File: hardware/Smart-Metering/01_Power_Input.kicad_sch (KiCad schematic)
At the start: 0 parts

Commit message: Implementa folha de entrada de energia e numera referências por folha
01_Power_Input:
- modo padrão: LINE_A/B/C -> fusível -> diodo S1M em OU para o
  barramento HV, retorno no NEUTRAL via JP101; o instrumento segue
  alimentado com qualquer fase presente;
- modo auxiliar (J101, 100-240 VAC, com varistor): F104/D104/JP102,
  não montados por padrão; para rede 3 fios sem neutro;
- R101 fusível limita inrush, C101 4,7 uF/450 V no barramento;
- PS101 módulo AC/DC isolado 5 V / 2 A (ex.: IRM-10-5) gerando
  VIN_ACDC para a folha 09, referenciado a GND_SYS.

Referências renumeradas por folha para evitar colisões: folha 02 passa
a 2xx (R201 = ligação neutro/GND), folha 03 a 3xx e folha 04 a 4xx
(U401 = ADE9430).

Novos símbolos: D_Rect, CP_Vert, Jumper_2 e ACDC_Module.

Co-Authored-By: Claude Opus 5.5 <noreply@anthropic.com>
Claude-Session: https://claude.ai/code/session_012B8cVkhtjf3eg98UdpNCpf
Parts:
- added C101: 4.7uF 450V, Capacitor_THT:CP_Radial_D8.0mm_P3.50mm, symbol SmartMetering:CP_Vert
- added C102: 22uF, Capacitor_SMD:C_1206_3216Metric, symbol SmartMetering:C_Vert
- added C103: 100nF, Capacitor_SMD:C_0603_1608Metric, symbol SmartMetering:C_Vert
- added D101, D102, D103, D104: S1M, Diode_SMD:D_SMA, symbol SmartMetering:D_Rect
- added F101, F102, F103, F104: T250mA 500VAC, symbol SmartMetering:Fuse
- added J101: AUX L N, TerminalBlock_Phoenix:TerminalBlock_Phoenix_MKDS-1,5-2-5.08_1x02_P5.08mm_Horizontal, symbol SmartMetering:Screw_Terminal_01x02
- added JP101, JP102: LINK, Resistor_THT:R_Axial_DIN0207_L6.3mm_D2.5mm_P7.62mm_Horizontal, symbol SmartMetering:Jumper_2
- added PS101: IRM-10-5, symbol SmartMetering:ACDC_Module
- added R101: 22R 2W, Resistor_THT:R_Axial_DIN0414_L11.9mm_D4.5mm_P15.24mm_Horizontal, symbol SmartMetering:R_Vert
- added RV101: 320VAC 14mm, symbol SmartMetering:Varistor
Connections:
- new net: C101.1 (+), PS101.1 (AC/L), R101.2
- new net: D103.2 (A), F103.2
- new net: D101.1 (K), D102.1 (K), D103.1 (K), D104.1 (K), R101.1
- new net: D102.2 (A), F102.2
- new net: D104.2 (A), F104.2
- new net: D101.2 (A), F101.2
- new net GND_SYS: C102.2, C103.2, PS101.3 (-V)
- new net HV_RTN: C101.2 (-), JP101.2, JP102.2, PS101.2 (AC/N)
- new net LINE_A: F101.1
- new net LINE_B: F102.1
- new net LINE_C: F103.1
- new net L_AUX: F104.1, J101.1, RV101.1
- new net NEUTRAL: JP101.1
- new net N_AUX: J101.2, JP102.1, RV101.2
- new net VIN_ACDC: C102.1, C103.1, PS101.4 (+V)
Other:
- note added: "ENTRADA DE ENERGIA DO INSTRUMENTO Modo padrão (pelas fases medidas): F101-F103 + D101-D103 + JP101 montados; F104/D104/JP102 não montados. O instrumento continua alimentado enquanto houver qualquer fase presente (OU de diodos, retorno no NEUTRO). Barramento HV ≈ 311 VDC com 220 V fase-neutro. Modo auxiliar (J101, 100-240 VAC): F104 + D104 + JP102 montados; F101-F103 e JP101 não montados. Use em r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"
- note added: "PS101: módulo AC/DC isolado (reforçado), 5 V / 2 A, aceita entrada CC 120-370 V. Ele é a barreira de isolação entre a rede e o domínio seguro (GND_SYS). Confirmar isolação e categoria de sobretensão do módulo para CAT III 300 V; a proteção de surto vem dos varistores (folha 02 e RV101) e de R101 (fusível, limita inrush). R101 e C101: limitam a corrente de partida e filtram o ripple do retificador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"
- company: (none) -> Smart-Metering
- title: (none) -> Power Input - AC/DC

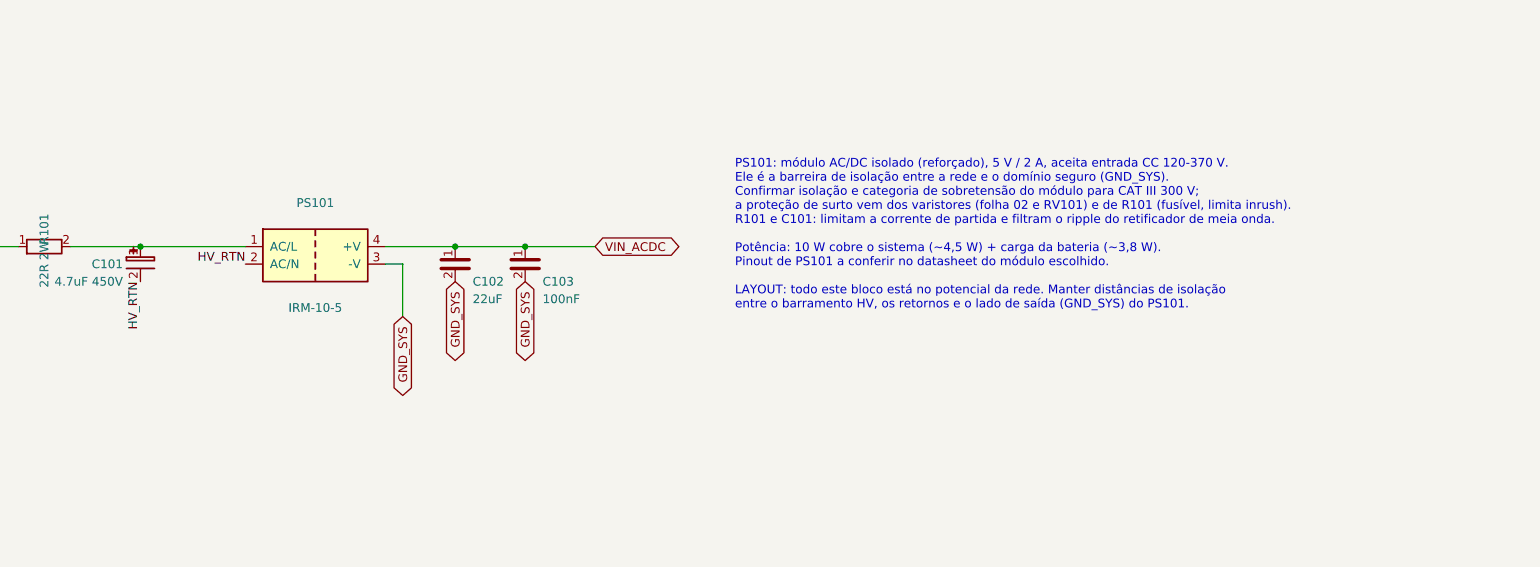
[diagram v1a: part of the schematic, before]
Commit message: Revisão completa do esquemático e correções
Verificação automática sobre o netlist global (215 componentes, 176 nets):
sem pinos soltos, sem nets de alimentação sem fonte, sem saídas em
conflito e isolação íntegra (terras só se encontram nas barreiras
PS101, PS601, U601, U602 e U801).

Correções:
- footprint do ADE9430 inexistente na biblioteca KiCad trocado por
  QFN-40 6x6 (tamanho do pad exposto a confirmar);
- MISO do ADE9430 como tri-state (barramento compartilhado com MCP3204);
- PS101 com símbolo e footprint oficiais do IRM-10-5 (o símbolo genérico
  tinha AC/L e AC/N trocados);
- PWR_FLAG em HV_DC, HV_RTN, VBAT_RTC, VDDA, GND_485 e VIN_CHG;
- footprints para fusíveis, varistores, indutores e chave de energia;
- polarização de fail-safe opcional no RS-485 (R807/R808, DNP);
- notas de layout (retorno do AC/DC) e de firmware (VBUS no PA9).

Relatório com revisão por folha, orçamento de potência e pendências em
docs/REVISAO_ESQUEMATICO.md.

Co-Authored-By: Claude Opus 5.5 <noreply@anthropic.com>
Claude-Session: https://claude.ai/code/session_012B8cVkhtjf3eg98UdpNCpf
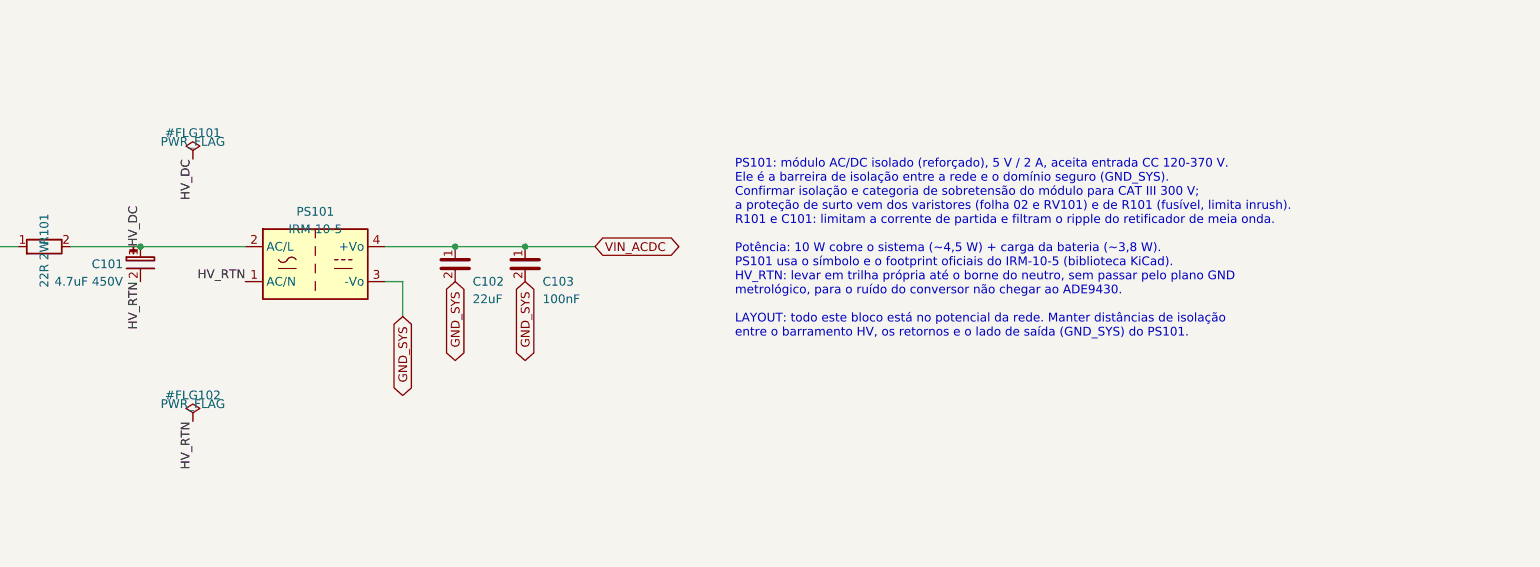
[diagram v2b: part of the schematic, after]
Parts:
- removed PS101: IRM-10-5, symbol SmartMetering:ACDC_Module
- added PS101: IRM-10-5, Converter_ACDC:Converter_ACDC_MeanWell_IRM-10-xx_THT, symbol Converter_ACDC:IRM-10-5
- F101, F102, F103, F104: footprint (none) -> Fuse:Fuseholder_Clip-5x20mm_Littelfuse_111_Inline_P20.00x5.00mm_D1.05mm_Horizontal
- RV101: footprint (none) -> Varistor:RV_Disc_D15.5mm_W4.5mm_P7.5mm
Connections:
- net GND_SYS: now also PS101.3 (-Vo)
- net HV_RTN: now also PS101.1 (AC/N)
- net VIN_ACDC: now also PS101.4 (+Vo)
- net HV_DC: now reaches C101.1 (+), R101.2
- net HV_DC: now also PS101.2 (AC/L)
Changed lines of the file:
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@@
 		(effects (font (size 1.27 1.27)) (justify left top))
 	)
-	(text "PS101: módulo AC/DC isolado (reforçado), 5 V / 2 A, aceita entrada CC 120-370 V.\nEle é a barreira de isolação entre a rede e o domínio seguro (GND_SYS).\nConfirmar isolação e categoria de sobretensão do módulo para CAT III 300 V;\na proteção de surto vem dos varistores (folha 02 e RV101) e de R101 (fusível, limita inrush).\nR101 e C101: limitam a corrente de partida e filtram o ripple do retificador de meia onda.\n\nPotência: 10 W cobre o sistema (~4,5 W) + carga da bateria (~3,8 W).\nPinout de PS101 a conferir no datasheet do módulo escolhido.\n\nLAYOUT: todo este bloco está no potencial da rede. Manter distâncias de isolação\nentre o barramento HV, os retornos e o lado de saída (GND_SYS) do PS101."
+	(text "PS101: módulo AC/DC isolado (reforçado), 5 V / 2 A, aceita entrada CC 120-370 V.\nEle é a barreira de isolação entre a rede e o domínio seguro (GND_SYS).\nConfirmar isolação e categoria de sobretensão do módulo para CAT III 300 V;\na proteção de surto vem dos varistores (folha 02 e RV101) e de R101 (fusível, limita inrush).\nR101 e C101: limitam a corrente de partida e filtram o ripple do retificador de meia onda.\n\nPotência: 10 W cobre o sistema (~4,5 W) + carga da bateria (~3,8 W).\nPS101 usa o símbolo e o footprint oficiais do IRM-10-5 (biblioteca KiCad).\nHV_RTN: levar em trilha própria até o borne do neutro, sem passar pelo plano GND\nmetrológico, para o ruído do conversor não chegar ao ADE9430.\n\nLAYOUT: todo este bloco está no potencial da rede. Manter distâncias de isolação\nentre o barramento HV, os retornos e o lado de saída (GND_SYS) do PS101."
 		(exclude_from_sim no)(at 200.66 88.9 0)
 		(effects (font (size 1.27 1.27)) (justify left top))
@@
 		(stroke (width 0) (type default))
 	)
-	(wire (pts (xy 149.86 104.14) (xy 152.4 104.14))
-		(stroke (width 0) (type default))
-	)
-	(wire (pts (xy 152.4 104.14) (xy 152.4 111.76))
+	(wire (pts (xy 149.86 106.68) (xy 152.4 106.68))
+		(stroke (width 0) (type default))
+	)
+	(wire (pts (xy 152.4 106.68) (xy 152.4 111.76))
 		(stroke (width 0) (type default))
 	)
@@
 		(effects (font (size 1.27 1.27)) (justify right bottom))
 	)
-	(label "HV_RTN" (at 129.54 104.14 180)
+	(label "HV_DC" (at 114.3 101.6 90)
+		(effects (font (size 1.27 1.27)) (justify left bottom))
+	)
+	(label "HV_DC" (at 121.92 88.9 270)
+		(effects (font (size 1.27 1.27)) (justify right bottom))
+	)
+	(label "HV_RTN" (at 121.92 127 270)
+		(effects (font (size 1.27 1.27)) (justify right bottom))
+	)
+	(label "HV_RTN" (at 129.54 106.68 180)
 		(effects (font (size 1.27 1.27)) (justify right bottom))
 	)
@@
 		(property "Reference" "F101" (at 63.5 48.26 0) (effects (font (size 1.27 1.27))))
 		(property "Value" "T250mA 500VAC" (at 63.5 53.34 0) (effects (font (size 1.27 1.27))))
-		(property "Footprint" "" (at 63.5 50.8 0) (effects (font (size 1.27 1.27)) (hide yes)))
+		(property "Footprint" "Fuse:Fuseholder_Clip-5x20mm_Littelfuse_111_Inline_P20.00x5.00mm_D1.05mm_Horizontal" (at 63.5 50.8 0) (effects (font (size 1.27 1.27)) (hide yes)))
 		(property "Datasheet" "" (at 63.5 50.8 0) (effects (font (size 1.27 1.27)) (hide yes)))
 		(property "Description" "Supply tap fuse, phase A, time-lag, >=500 VAC" (at 63.5 50.8 0) (effects (font (size 1.27 1.27)) (hide yes)))
@@
 		(property "Reference" "F102" (at 63.5 60.96 0) (effects (font (size 1.27 1.27))))
 		(property "Value" "T250mA 500VAC" (at 63.5 66.04 0) (effects (font (size 1.27 1.27))))
-		(property "Footprint" "" (at 63.5 63.5 0) (effects (font (size 1.27 1.27)) (hide yes)))
+		(property "Footprint" "Fuse:Fuseholder_Clip-5x20mm_Littelfuse_111_Inline_P20.00x5.00mm_D1.05mm_Horizontal" (at 63.5 63.5 0) (effects (font (size 1.27 1.27)) (hide yes)))
 		(property "Datasheet" "" (at 63.5 63.5 0) (effects (font (size 1.27 1.27)) (hide yes)))
 		(property "Description" "Supply tap fuse, phase B, time-lag, >=500 VAC" (at 63.5 63.5 0) (effects (font (size 1.27 1.27)) (hide yes)))
@@
 		(property "Reference" "F103" (at 63.5 73.66 0) (effects (font (size 1.27 1.27))))
 		(property "Value" "T250mA 500VAC" (at 63.5 78.74 0) (effects (font (size 1.27 1.27))))
-		(property "Footprint" "" (at 63.5 76.2 0) (effects (font (size 1.27 1.27)) (hide yes)))
+		(property "Footprint" "Fuse:Fuseholder_Clip-5x20mm_Littelfuse_111_Inline_P20.00x5.00mm_D1.05mm_Horizontal" (at 63.5 76.2 0) (effects (font (size 1.27 1.27)) (hide yes)))
 		(property "Datasheet" "" (at 63.5 76.2 0) (effects (font (size 1.27 1.27)) (hide yes)))
 		(property "Description" "Supply tap fuse, phase C, time-lag, >=500 VAC" (at 63.5 76.2 0) (effects (font (size 1.27 1.27)) (hide yes)))
@@
 		(property "Reference" "F104" (at 63.5 99.06 0) (effects (font (size 1.27 1.27))))
 		(property "Value" "T250mA 500VAC" (at 63.5 104.14 0) (effects (font (size 1.27 1.27))))
-		(property "Footprint" "" (at 63.5 101.6 0) (effects (font (size 1.27 1.27)) (hide yes)))
+		(property "Footprint" "Fuse:Fuseholder_Clip-5x20mm_Littelfuse_111_Inline_P20.00x5.00mm_D1.05mm_Horizontal" (at 63.5 101.6 0) (effects (font (size 1.27 1.27)) (hide yes)))
 		(property "Datasheet" "" (at 63.5 101.6 0) (effects (font (size 1.27 1.27)) (hide yes)))
 		(property "Description" "Auxiliary input fuse, time-lag, >=500 VAC" (at 63.5 101.6 0) (effects (font (size 1.27 1.27)) (hide yes)))
@@
 	)
 	(symbol
-		(lib_id "SmartMetering:ACDC_Module")
-		(at 139.7 102.87 0)
-		(unit 1)(body_style 1)
-		(exclude_from_sim no)(in_bom yes)(on_board yes)(in_pos_files yes)(dnp no)
-		(property "Reference" "PS101" (at 139.7 95.25 0) (effects (font (size 1.27 1.27))))
-		(property "Value" "IRM-10-5" (at 139.7 110.49 0) (effects (font (size 1.27 1.27))))
-		(property "Footprint" "" (at 139.7 102.87 0) (effects (font (size 1.27 1.27)) (hide yes)))
-		(property "Datasheet" "" (at 139.7 102.87 0) (effects (font (size 1.27 1.27)) (hide yes)))
-		(property "Description" "AC/DC 5 V 2 A, 85-264 VAC / 120-370 VDC input, reinforced (e.g. Mean Well IRM-10-5); verify pinout" (at 139.7 102.87 0) (effects (font (size 1.27 1.27)) (hide yes)))
-		(pin "1")
-		(pin "2")
+		(lib_id "power:PWR_FLAG")
+		(at 121.92 88.9 0)
+		(unit 1)(body_style 1)
+		(exclude_from_sim no)(in_bom yes)(on_board yes)(in_pos_files yes)(dnp no)
+		(property "Reference" "#FLG101" (at 121.92 85.09 0) (effects (font (size 1.27 1.27))))
+		(property "Value" "PWR_FLAG" (at 121.92 86.36 0) (effects (font (size 1.27 1.27))))
+		(property "Footprint" "" (at 121.92 88.9 0) (effects (font (size 1.27 1.27)) (hide yes)))
+		(property "Datasheet" "" (at 121.92 88.9 0) (effects (font (size 1.27 1.27)) (hide yes)))
+		(property "Description" "" (at 121.92 88.9 0) (effects (font (size 1.27 1.27)) (hide yes)))
+		(pin "1")
+		(instances
+			(project "Smart-Metering"
+				(path "/5fa62d70-4279-48bb-8603-6bcc60fb353a/a10e1001-0001-4e01-9001-000000000001" (reference "#FLG101") (unit 1))
+			)
+		)
+	)
+	(symbol
+		(lib_id "power:PWR_FLAG")
+		(at 121.92 127 0)
+		(unit 1)(body_style 1)
+		(exclude_from_sim no)(in_bom yes)(on_board yes)(in_pos_files yes)(dnp no)
+		(property "Reference" "#FLG102" (at 121.92 123.19 0) (effects (font (size 1.27 1.27))))
+		(property "Value" "PWR_FLAG" (at 121.92 124.46 0) (effects (font (size 1.27 1.27))))
+		(property "Footprint" "" (at 121.92 127 0) (effects (font (size 1.27 1.27)) (hide yes)))
+		(property "Datasheet" "" (at 121.92 127 0) (effects (font (size 1.27 1.27)) (hide yes)))
+		(property "Description" "" (at 121.92 127 0) (effects (font (size 1.27 1.27)) (hide yes)))
+		(pin "1")
+		(instances
+			(project "Smart-Metering"
+				(path "/5fa62d70-4279-48bb-8603-6bcc60fb353a/a10e1001-0001-4e01-9001-000000000001" (reference "#FLG102") (unit 1))
+			)
+		)
+	)
+	(symbol
+		(lib_id "Converter_ACDC:IRM-10-5")
+		(at 139.7 104.14 0)
+		(unit 1)(body_style 1)
+		(exclude_from_sim no)(in_bom yes)(on_board yes)(in_pos_files yes)(dnp no)
+		(property "Reference" "PS101" (at 139.7 96.52 0) (effects (font (size 1.27 1.27))))
+		(property "Value" "IRM-10-5" (at 139.7 99.06 0) (effects (font (size 1.27 1.27))))
+		(property "Footprint" "Converter_ACDC:Converter_ACDC_MeanWell_IRM-10-xx_THT" (at 139.7 104.14 0) (effects (font (size 1.27 1.27)) (hide yes)))
+		(property "Datasheet" "" (at 139.7 104.14 0) (effects (font (size 1.27 1.27)) (hide yes)))
+		(property "Description" "AC/DC 5 V 2 A, 85-264 VAC / 120-370 VDC input, reinforced (Mean Well IRM-10-5)" (at 139.7 104.14 0) (effects (font (size 1.27 1.27)) (hide yes)))
+		(pin "1")
+		(pin "2")
+		(pin "3")
 		(pin "4")
-		(pin "3")
 		(instances
 			(project "Smart-Metering"
@@
 		(property "Reference" "RV101" (at 53.34 125.73 0) (effects (font (size 1.27 1.27)) (justify left)))
 		(property "Value" "320VAC 14mm" (at 53.34 128.27 0) (effects (font (size 1.27 1.27)) (justify left)))
-		(property "Footprint" "" (at 50.8 127 0) (effects (font (size 1.27 1.27)) (hide yes)))
+		(property "Footprint" "Varistor:RV_Disc_D15.5mm_W4.5mm_P7.5mm" (at 50.8 127 0) (effects (font (size 1.27 1.27)) (hide yes)))
 		(property "Datasheet" "" (at 50.8 127 0) (effects (font (size 1.27 1.27)) (hide yes)))
 		(property "Description" "Auxiliary input MOV (e.g. S14K320)" (at 50.8 127 0) (effects (font (size 1.27 1.27)) (hide yes)))
